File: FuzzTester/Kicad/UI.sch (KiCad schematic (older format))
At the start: 6 parts, among them J10 Key Pad JST XH, J11 1602 LCD JST XH

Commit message: PCB fixes
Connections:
- wire segments 11 -> 14
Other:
- moved on the sheet: R6, R7, R8
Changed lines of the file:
@@
 encoding utf-8
 Sheet 4 10
-Title ""
+Title "Guitar Pedal Effect Fuzz Digitally Controlled"
 Date ""
-Rev ""
+Rev "0.1"
 Comp ""
 Comment1 ""
@@
 L Device:R R?
 U 1 1 5E8FB44D
-P 3100 2300
+P 2950 2300
 AR Path="/5E8FB44D" Ref="R?"  Part="1"
 AR Path="/5E8F7778/5E8FB44D" Ref="R8"  Part="1"
-F 0 "R8" V 2893 2300 50  0000 C CNN
-F 1 "1K" V 2984 2300 50  0000 C CNN
-F 2 "Resistor_SMD:R_0805_2012Metric_Pad1.15x1.40mm_HandSolder" V 3030 2300 50  0001 C CNN
-F 3 "~" H 3100 2300 50  0001 C CNN
-	1    3100 2300
+F 0 "R8" V 2900 2450 50  0000 C CNN
+F 1 "1K" V 2950 2300 50  0000 C CNN
+F 2 "Resistor_SMD:R_0805_2012Metric_Pad1.15x1.40mm_HandSolder" V 2880 2300 50  0001 C CNN
+F 3 "~" H 2950 2300 50  0001 C CNN
+	1    2950 2300
 	0    1    1    0
 $EndComp
@@
 L Device:R R?
 U 1 1 5E8FB453
-P 2750 2400
+P 2600 2400
 AR Path="/5E8FB453" Ref="R?"  Part="1"
 AR Path="/5E8F7778/5E8FB453" Ref="R7"  Part="1"
-F 0 "R7" V 2543 2400 50  0000 C CNN
-F 1 "1K" V 2634 2400 50  0000 C CNN
-F 2 "Resistor_SMD:R_0805_2012Metric_Pad1.15x1.40mm_HandSolder" V 2680 2400 50  0001 C CNN
-F 3 "~" H 2750 2400 50  0001 C CNN
-	1    2750 2400
+F 0 "R7" V 2550 2550 50  0000 C CNN
+F 1 "1K" V 2600 2400 50  0000 C CNN
+F 2 "Resistor_SMD:R_0805_2012Metric_Pad1.15x1.40mm_HandSolder" V 2530 2400 50  0001 C CNN
+F 3 "~" H 2600 2400 50  0001 C CNN
+	1    2600 2400
 	0    1    1    0
 $EndComp
@@
 L Device:R R?
 U 1 1 5E8FB459
-P 2350 2500
+P 2250 2500
 AR Path="/5E8FB459" Ref="R?"  Part="1"
 AR Path="/5E8F7778/5E8FB459" Ref="R6"  Part="1"
-F 0 "R6" V 2143 2500 50  0000 C CNN
-F 1 "1K" V 2234 2500 50  0000 C CNN
-F 2 "Resistor_SMD:R_0805_2012Metric_Pad1.15x1.40mm_HandSolder" V 2280 2500 50  0001 C CNN
-F 3 "~" H 2350 2500 50  0001 C CNN
-	1    2350 2500
+F 0 "R6" V 2200 2650 50  0000 C CNN
+F 1 "1K" V 2250 2500 50  0000 C CNN
+F 2 "Resistor_SMD:R_0805_2012Metric_Pad1.15x1.40mm_HandSolder" V 2180 2500 50  0001 C CNN
+F 3 "~" H 2250 2500 50  0001 C CNN
+	1    2250 2500
 	0    1    1    0
 $EndComp
@@
 AR Path="/5E8FB45F" Ref="R?"  Part="1"
 AR Path="/5E8F7778/5E8FB45F" Ref="R5"  Part="1"
-F 0 "R5" V 1693 2600 50  0000 C CNN
-F 1 "1K" V 1784 2600 50  0000 C CNN
+F 0 "R5" V 1850 2750 50  0000 C CNN
+F 1 "1K" V 1900 2600 50  0000 C CNN
 F 2 "Resistor_SMD:R_0805_2012Metric_Pad1.15x1.40mm_HandSolder" V 1830 2600 50  0001 C CNN
 F 3 "~" H 1900 2600 50  0001 C CNN
@@
 $EndComp
 Wire Wire Line
-	2600 2400 1800 2400
+	2450 2400 1800 2400
 Wire Wire Line
-	1800 2500 2200 2500
+	1700 2500 1800 2500
 Wire Wire Line
 	1800 2600 1750 2600
@@
 Text HLabel 1800 2200 2    50   Input ~ 0
 GPIO_KEYPAD_ROW_4
-Text HLabel 3250 2300 2    50   Input ~ 0
+Text HLabel 3100 2300 2    50   Input ~ 0
 GPIO_KEYPAD_COLUMN_1
-Text HLabel 3250 2400 2    50   Input ~ 0
+Text HLabel 3100 2400 2    50   Input ~ 0
 GPIO_KEYPAD_COLUMN_2
-Text HLabel 3250 2500 2    50   Input ~ 0
+Text HLabel 3100 2500 2    50   Input ~ 0
 GPIO_KEYPAD_COLUMN_3
-Text HLabel 3250 2600 2    50   Input ~ 0
+Text HLabel 3100 2600 2    50   Input ~ 0
 GPIO_KEYPAD_COLUMN_4
 Wire Wire Line
-	1800 2300 2950 2300
+	1800 2300 2800 2300
 Wire Wire Line
-	3250 2400 2900 2400
+	3100 2400 2750 2400
 Wire Wire Line
-	2500 2500 3250 2500
+	2400 2500 3100 2500
 Wire Wire Line
-	3250 2600 2050 2600
+	3100 2600 2050 2600
+Connection ~ 1800 2400
+Wire Wire Line
+	1800 2400 1700 2400
+Connection ~ 1800 2500
+Wire Wire Line
+	1800 2500 2100 2500
+Connection ~ 2050 2600
+Wire Wire Line
+	2050 2600 1950 2600
 $EndSCHEMATC

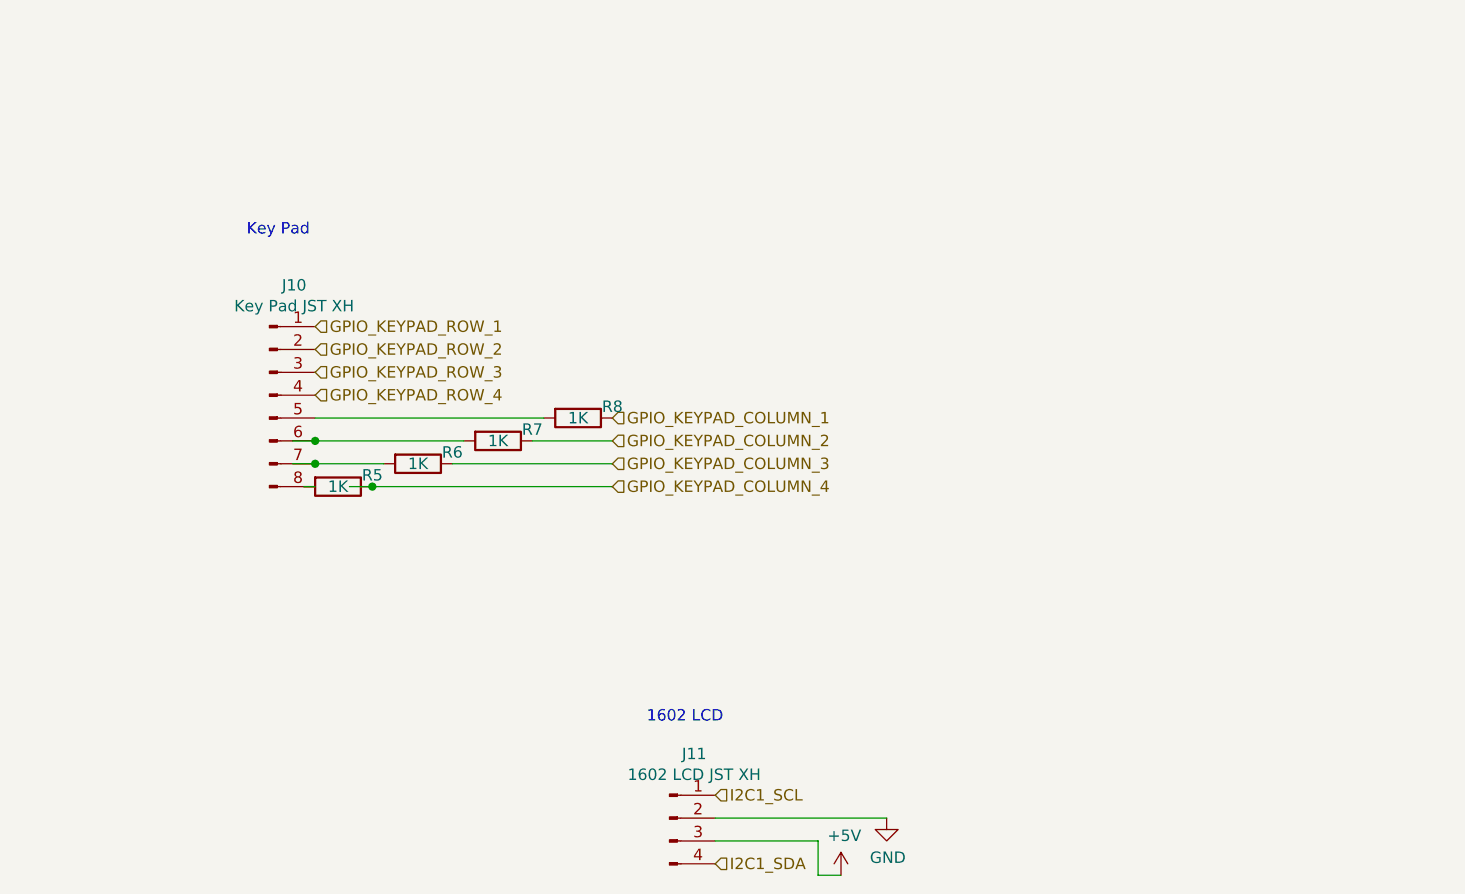
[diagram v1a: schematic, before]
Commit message: Schematics UI/MCU -> MCU + PCB improvements
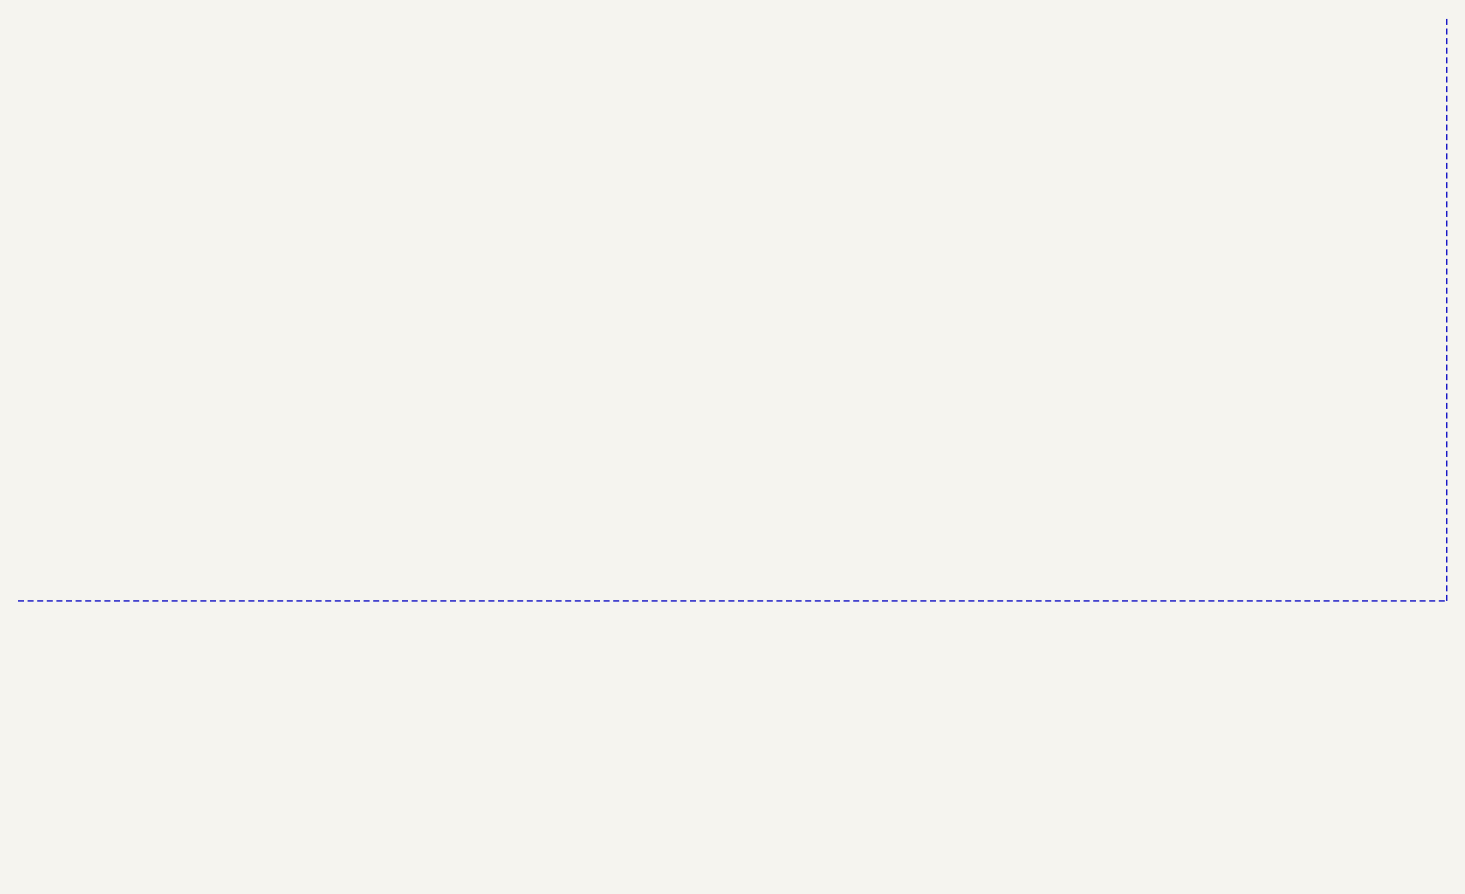
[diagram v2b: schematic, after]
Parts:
- removed J10: Key Pad JST XH, Connector_JST:JST_XH_B8B-XH-A_1x08_P2.50mm_Vertical, symbol Connector:Conn_01x08_Male
- removed J11: 1602 LCD JST XH, Connector_JST:JST_XH_B4B-XH-A_1x04_P2.50mm_Vertical, symbol Connector:Conn_01x04_Male
- removed R5, R6, R7, R8: 1K, Resistor_SMD:R_0805_2012Metric_Pad1.15x1.40mm_HandSolder, symbol Device:R
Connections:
- net labels removed: +5V, GND, GPIO_KEYPAD_COLUMN_1, GPIO_KEYPAD_COLUMN_2, GPIO_KEYPAD_COLUMN_3, GPIO_KEYPAD_COLUMN_4, GPIO_KEYPAD_ROW_1, GPIO_KEYPAD_ROW_2, GPIO_KEYPAD_ROW_3, GPIO_KEYPAD_ROW_4, I2C1_SCL, I2C1_SDA
- wire segments 14 -> 0
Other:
- note removed: "1602 LCD\n\n\n"
- note removed: "Key Pad\n\n\n\n"
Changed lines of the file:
@@
 Sheet 4 10
 Title "Guitar Pedal Effect Fuzz Digitally Controlled"
-Date ""
+Date "2020-04-07"
 Rev "0.1"
-Comp ""
+Comp "Michel Keijzers"
 Comment1 ""
-Comment2 ""
-Comment3 ""
-Comment4 ""
+Comment2 "and 2 sets of 8 capacitors"
+Comment3 "Pedal Effect Fuzz based on 2 sets of 20 different transistors"
+Comment4 "User Interface (1602 LED Display and 4x4 Keypad)"
 $EndDescr
-$Comp
-L Connector:Conn_01x08_Male J?
-U 1 1 5E8FB442
-P 1600 2200
-AR Path="/5E8FB442" Ref="J?"  Part="1"
-AR Path="/5E8F7778/5E8FB442" Ref="J10"  Part="1"
-F 0 "J10" H 1708 2681 50  0000 C CNN
-F 1 "Key Pad JST XH" H 1708 2590 50  0000 C CNN
-F 2 "Connector_JST:JST_XH_B8B-XH-A_1x08_P2.50mm_Vertical" H 1600 2200 50  0001 C CNN
-F 3 "~" H 1600 2200 50  0001 C CNN
-	1    1600 2200
-	1    0    0    -1
-$EndComp
-$Comp
-L Device:R R?
-U 1 1 5E8FB44D
-P 2950 2300
-AR Path="/5E8FB44D" Ref="R?"  Part="1"
-AR Path="/5E8F7778/5E8FB44D" Ref="R8"  Part="1"
-F 0 "R8" V 2900 2450 50  0000 C CNN
-F 1 "1K" V 2950 2300 50  0000 C CNN
-F 2 "Resistor_SMD:R_0805_2012Metric_Pad1.15x1.40mm_HandSolder" V 2880 2300 50  0001 C CNN
-F 3 "~" H 2950 2300 50  0001 C CNN
-	1    2950 2300
-	0    1    1    0
-$EndComp
-$Comp
-L Device:R R?
-U 1 1 5E8FB453
-P 2600 2400
-AR Path="/5E8FB453" Ref="R?"  Part="1"
-AR Path="/5E8F7778/5E8FB453" Ref="R7"  Part="1"
-F 0 "R7" V 2550 2550 50  0000 C CNN
-F 1 "1K" V 2600 2400 50  0000 C CNN
-F 2 "Resistor_SMD:R_0805_2012Metric_Pad1.15x1.40mm_HandSolder" V 2530 2400 50  0001 C CNN
-F 3 "~" H 2600 2400 50  0001 C CNN
-	1    2600 2400
-	0    1    1    0
-$EndComp
-$Comp
-L Device:R R?
-U 1 1 5E8FB459
-P 2250 2500
-AR Path="/5E8FB459" Ref="R?"  Part="1"
-AR Path="/5E8F7778/5E8FB459" Ref="R6"  Part="1"
-F 0 "R6" V 2200 2650 50  0000 C CNN
-F 1 "1K" V 2250 2500 50  0000 C CNN
-F 2 "Resistor_SMD:R_0805_2012Metric_Pad1.15x1.40mm_HandSolder" V 2180 2500 50  0001 C CNN
-F 3 "~" H 2250 2500 50  0001 C CNN
-	1    2250 2500
-	0    1    1    0
-$EndComp
-$Comp
-L Device:R R?
-U 1 1 5E8FB45F
-P 1900 2600
-AR Path="/5E8FB45F" Ref="R?"  Part="1"
-AR Path="/5E8F7778/5E8FB45F" Ref="R5"  Part="1"
-F 0 "R5" V 1850 2750 50  0000 C CNN
-F 1 "1K" V 1900 2600 50  0000 C CNN
-F 2 "Resistor_SMD:R_0805_2012Metric_Pad1.15x1.40mm_HandSolder" V 1830 2600 50  0001 C CNN
-F 3 "~" H 1900 2600 50  0001 C CNN
-	1    1900 2600
-	0    1    1    0
-$EndComp
-Wire Wire Line
-	2450 2400 1800 2400
-Wire Wire Line
-	1700 2500 1800 2500
-Wire Wire Line
-	1800 2600 1750 2600
-$Comp
-L Connector:Conn_01x04_Male J?
-U 1 1 5E8FB473
-P 3350 4050
-AR Path="/5E8FB473" Ref="J?"  Part="1"
-AR Path="/5E8F7778/5E8FB473" Ref="J11"  Part="1"
-F 0 "J11" H 3458 4331 50  0000 C CNN
-F 1 "1602 LCD JST XH" H 3458 4240 50  0000 C CNN
-F 2 "Connector_JST:JST_XH_B4B-XH-A_1x04_P2.50mm_Vertical" H 3350 4050 50  0001 C CNN
-F 3 "~" H 3350 4050 50  0001 C CNN
-	1    3350 4050
-	1    0    0    -1
-$EndComp
-$Comp
-L power:GND #PWR?
-U 1 1 5E8FB479
-P 4300 4050
-AR Path="/5E8FB479" Ref="#PWR?"  Part="1"
-AR Path="/5E8F7778/5E8FB479" Ref="#PWR027"  Part="1"
-F 0 "#PWR027" H 4300 3800 50  0001 C CNN
-F 1 "GND" H 4305 3877 50  0000 C CNN
-F 2 "" H 4300 4050 50  0001 C CNN
-F 3 "" H 4300 4050 50  0001 C CNN
-	1    4300 4050
-	1    0    0    -1
-$EndComp
-$Comp
-L power:+5V #PWR?
-U 1 1 5E8FB47F
-P 4100 4300
-AR Path="/5E8FB47F" Ref="#PWR?"  Part="1"
-AR Path="/5E8F7778/5E8FB47F" Ref="#PWR026"  Part="1"
-F 0 "#PWR026" H 4100 4150 50  0001 C CNN
-F 1 "+5V" H 4115 4473 50  0000 C CNN
-F 2 "" H 4100 4300 50  0001 C CNN
-F 3 "" H 4100 4300 50  0001 C CNN
-	1    4100 4300
-	1    0    0    -1
-$EndComp
-Text Notes 1500 1750 0    50   ~ 0
-Key Pad\n\n\n\n
-Text Notes 3250 3800 0    50   ~ 0
-1602 LCD\n\n\n
-Wire Wire Line
-	3550 4050 4300 4050
-Wire Wire Line
-	3550 4150 4000 4150
-Wire Wire Line
-	4000 4150 4000 4300
-Wire Wire Line
-	4000 4300 4100 4300
-Text HLabel 3550 3950 2    50   Input ~ 0
-I2C1_SCL
-Text HLabel 3550 4250 2    50   Input ~ 0
-I2C1_SDA
-Text HLabel 1800 1900 2    50   Input ~ 0
-GPIO_KEYPAD_ROW_1
-Text HLabel 1800 2000 2    50   Input ~ 0
-GPIO_KEYPAD_ROW_2
-Text HLabel 1800 2100 2    50   Input ~ 0
-GPIO_KEYPAD_ROW_3
-Text HLabel 1800 2200 2    50   Input ~ 0
-GPIO_KEYPAD_ROW_4
-Text HLabel 3100 2300 2    50   Input ~ 0
-GPIO_KEYPAD_COLUMN_1
-Text HLabel 3100 2400 2    50   Input ~ 0
-GPIO_KEYPAD_COLUMN_2
-Text HLabel 3100 2500 2    50   Input ~ 0
-GPIO_KEYPAD_COLUMN_3
-Text HLabel 3100 2600 2    50   Input ~ 0
-GPIO_KEYPAD_COLUMN_4
-Wire Wire Line
-	1800 2300 2800 2300
-Wire Wire Line
-	3100 2400 2750 2400
-Wire Wire Line
-	2400 2500 3100 2500
-Wire Wire Line
-	3100 2600 2050 2600
-Connection ~ 1800 2400
-Wire Wire Line
-	1800 2400 1700 2400
-Connection ~ 1800 2500
-Wire Wire Line
-	1800 2500 2100 2500
-Connection ~ 2050 2600
-Wire Wire Line
-	2050 2600 1950 2600
+Wire Notes Line
+	500  3100 6750 3100
+Wire Notes Line
+	6750 3100 6750 550
 $EndSCHEMATC
